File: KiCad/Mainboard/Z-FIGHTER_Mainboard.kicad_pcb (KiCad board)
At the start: 2 copper layers, 100 x 150 mm, 53 parts, among them IC1 Z80SIO, J1 DB9_Male_MountingHoles, J2 DB9_Male_MountingHoles, J3 USB_B, J4 Conn_02x13_Odd_Even, J5 Conn_Parallel_User, J6 Conn_PATA, J7 Conn_02x03_Odd_Even, SW1 SW_Push, SW2 SW_DIP_x03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

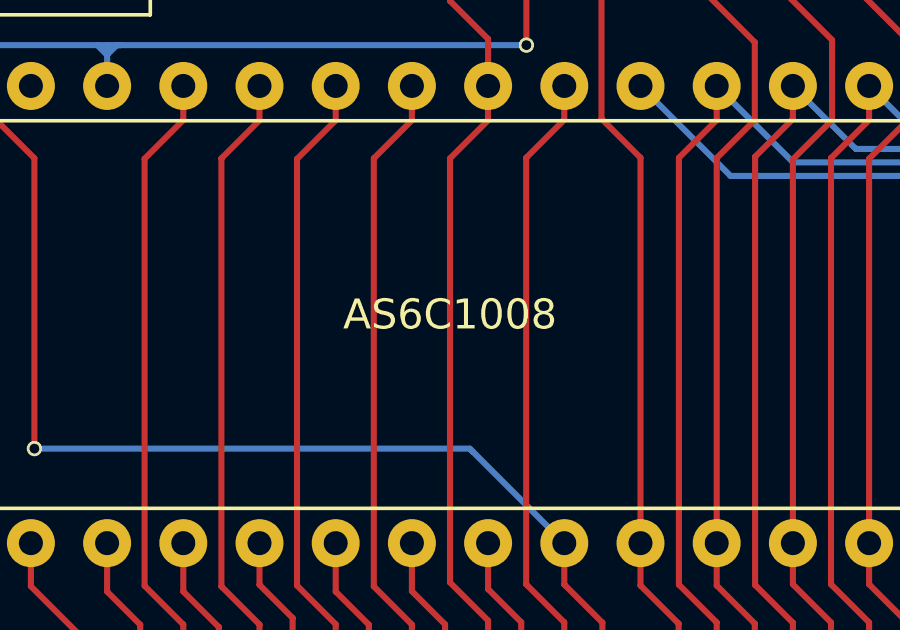
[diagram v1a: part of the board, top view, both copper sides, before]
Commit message: Changed SRAM silkscreen back to '4008
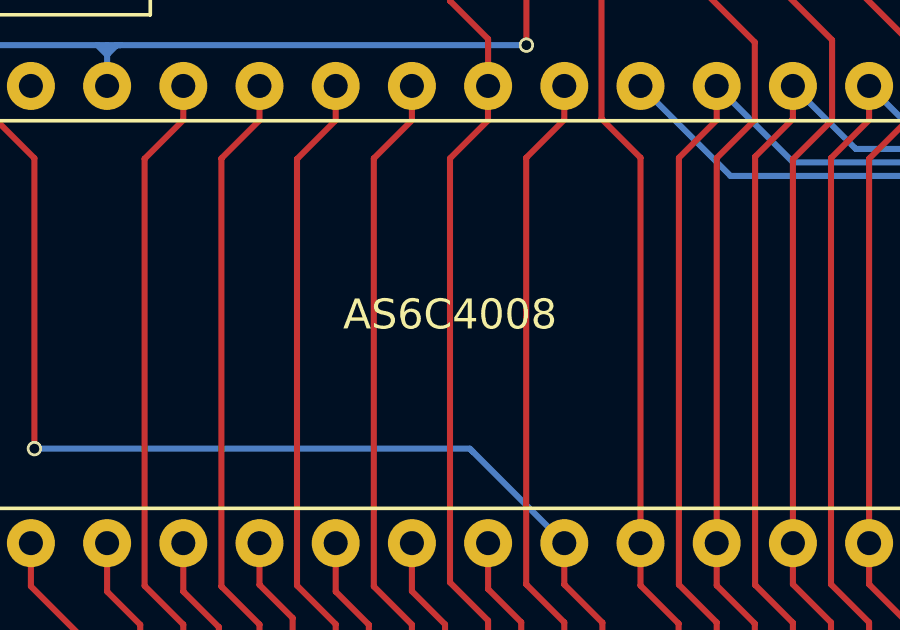
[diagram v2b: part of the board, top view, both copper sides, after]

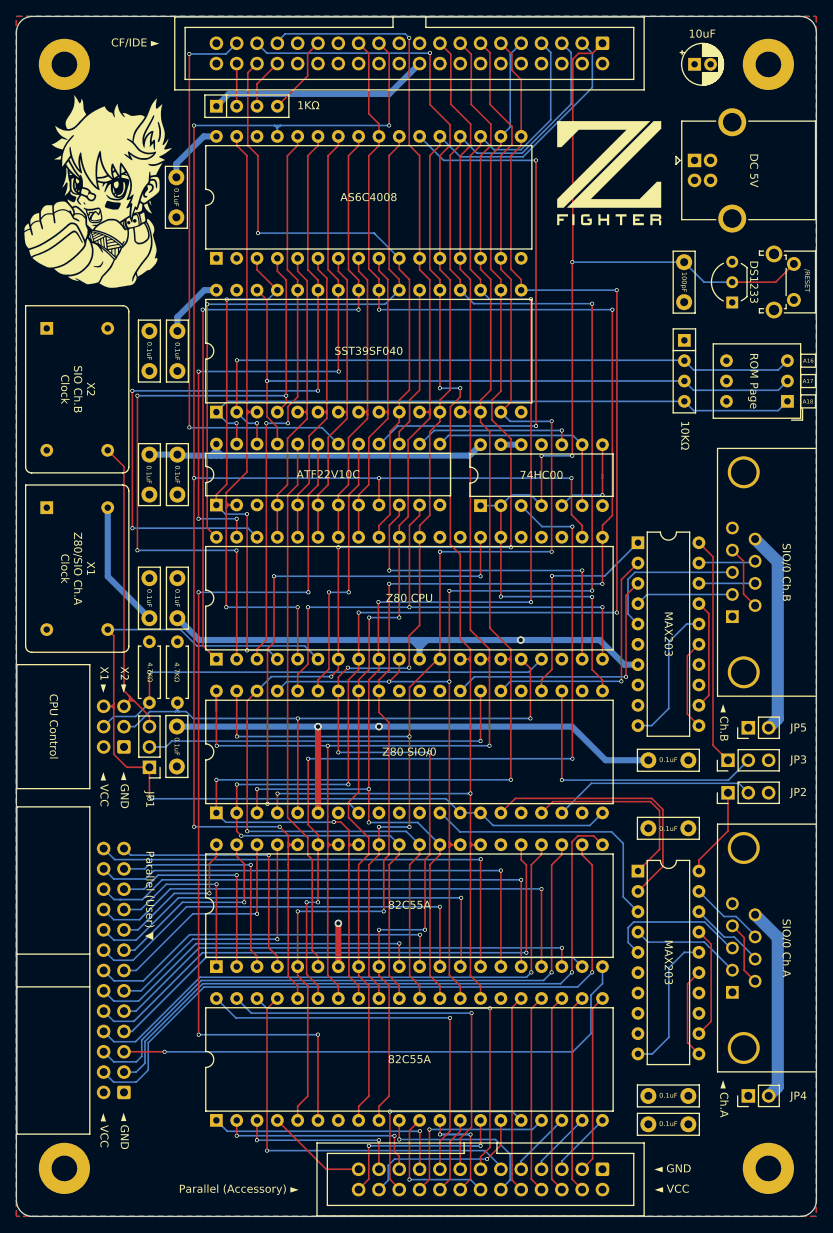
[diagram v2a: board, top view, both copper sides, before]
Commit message: Mainboard improvements
Support for DIP-8 oscillators, replaced system clock pin on CPU control header with CPU #WAIT, added jumper to select internal/external CLOCK2
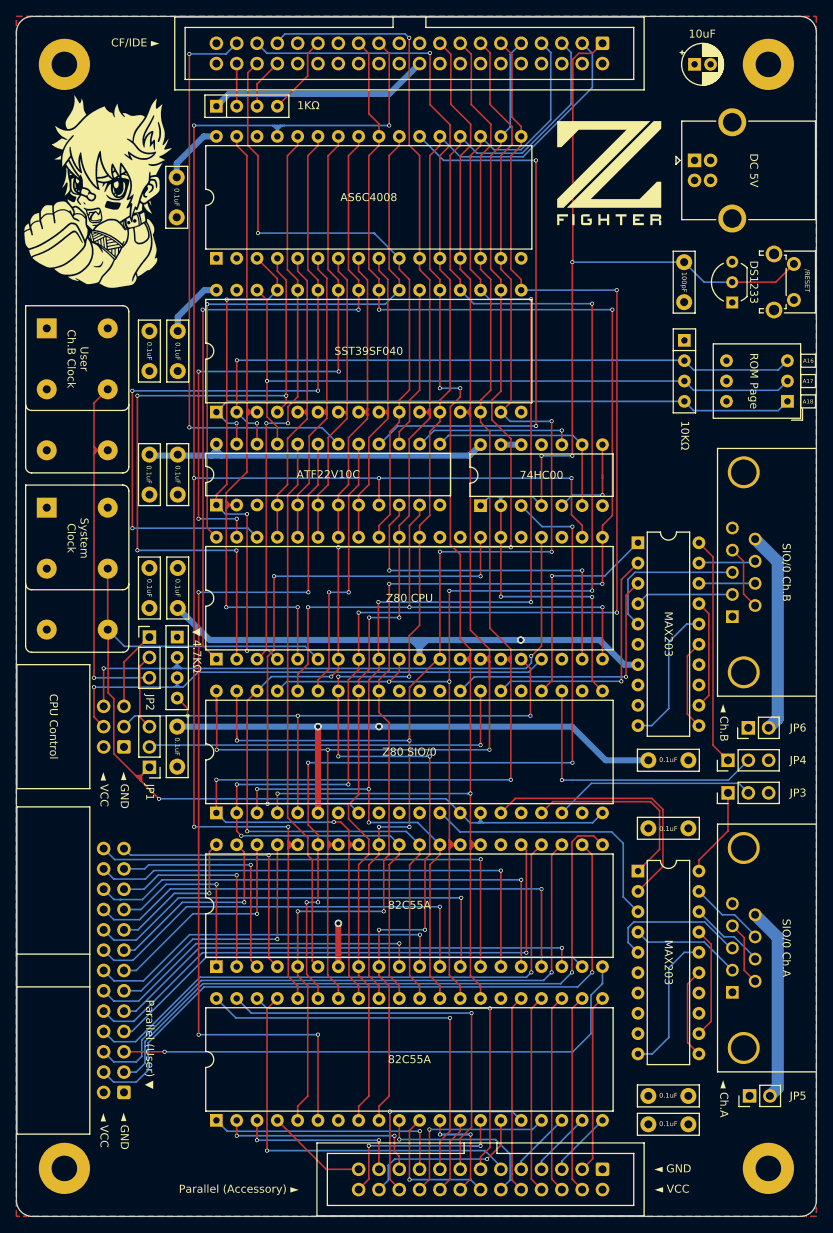
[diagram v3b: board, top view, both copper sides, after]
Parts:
- removed R1, R2: 4.7KΩ, Resistor_THT:R_Axial_DIN0207_L6.3mm_D2.5mm_P7.62mm_Horizontal
- added JP6: Jumper_2_Open, Connector_PinHeader_2.54mm:PinHeader_1x02_P2.54mm_Vertical, F.Cu at (159.4, 115.9)
- added REF**: Oscillator_DIP-8_LargePads, Oscillator:Oscillator_DIP-8_LargePads, F.Cu at (71.7, 88.4)
- added REF**: Oscillator_DIP-8_LargePads, Oscillator:Oscillator_DIP-8_LargePads, F.Cu at (71.7, 66.0)
- added ▼ 4.7KΩ: 4.7KΩ, Resistor_THT:R_Array_SIP4, F.Cu at (88.0, 104.6)
- JP4: value Jumper_2_Open -> Jumper_3_Open; footprint Connector_PinHeader_2.54mm:PinHeader_1x02_P2.54mm_Vertical -> Connector_PinHeader_2.54mm:PinHeader_1x03_P2.54mm_Vertical
- U1: value AS6C1008-55PCN -> AS6C4008-55PCN
- X1, X2: footprint Oscillator:Oscillator_DIP-14 -> Oscillator:Oscillator_DIP-14_LargePads
- moved JP2 74.9 mm to (84.5, 104.6), turned to 0 degrees
- moved JP5 46.0 mm to (159.6, 161.9)
- moved JP4 42.0 mm to (156.9, 120.0)
- moved JP3 4.08 mm to (156.9, 124.1)
- moved C8 1.27 mm to (88.1, 101.0)
- moved C3 1.27 mm to (84.5, 101.0)
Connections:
- net SIOCLOCKB renamed CLOCK_Ch.B
- IC1 pad 13: CLOCK1 -> CLOCK
- IC1 pad 14: CLOCK1 -> CLOCK
- IC1 pad 20: CLOCK1 -> CLOCK
- J7 pad 5: CLOCK2 -> CLOCK2_EXT
- J7 pad 6: CLOCK1 -> #WAIT
- JP1 pad 1: CLOCK1 -> CLOCK
- JP1 pad 3: CLOCK2 -> CLOCK2_USER
- JP2 pad 1: CTSA -> CLOCK2_EXT
- JP2 pad 2: SIO_CTSA -> CLOCK2_USER
- JP2 pad 3: GND -> CLOCK2
- JP3 pad 1: CTSB -> CTSA
- JP3 pad 2: SIO_CTSB -> SIO_CTSA
- JP4 pad 1: VCC -> CTSB
- JP4 pad 2: Net-(J1-Pad9) -> SIO_CTSB
- JP5 pad 2: Net-(J2-Pad9) -> Net-(J1-Pad9)
- U2 pad 24: VCC -> #WAIT
- U2 pad 6: CLOCK1 -> CLOCK
- X1 pad 8: CLOCK1 -> CLOCK
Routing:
- net CLOCK: track 0.00 -> 124.7 mm, vias 0 -> 1
- net CLOCK1: track 113.3 -> 0.00 mm, vias 1 -> 0
- net #WAIT: track 0.00 -> 80.8 mm, vias 0 -> 2
- net VCC: track 242.6 -> 227.0 mm
- net D0: track 173.3 -> 183.3 mm
- net CLOCK2_EXT: track 0.00 -> 9.97 mm
- net CLOCK2_USER: track 0.00 -> 9.64 mm
- net CLOCK2: track 39.4 -> 48.5 mm, vias 0 -> 1
- net D7: track 174.2 -> 182.5 mm
- net #WR: track 218.8 -> 225.8 mm
- net D1: track 180.6 -> 186.2 mm
- net A15: track 80.3 -> 85.0 mm
- net #NMI: track 60.8 -> 65.2 mm
- net #RESET: track 137.6 -> 141.0 mm
- net D6: track 195.9 -> 199.2 mm
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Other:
- board text added: "Mainboard Rev. 2b"
- board text added: "System Clock"
- board text added: "User Ch.B Clock"
- board text removed: "Mainboard Rev. 2a"
- board text removed: "X1 Z80/SIO Ch.A Clock"
- board text removed: "X1 ►"
- board text removed: "X2 SIO Ch.B Clock"
- board text removed: "X2 ►"

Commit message: Gerber settings
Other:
- rule pad_to_mask_clearance: 0.051 -> 0

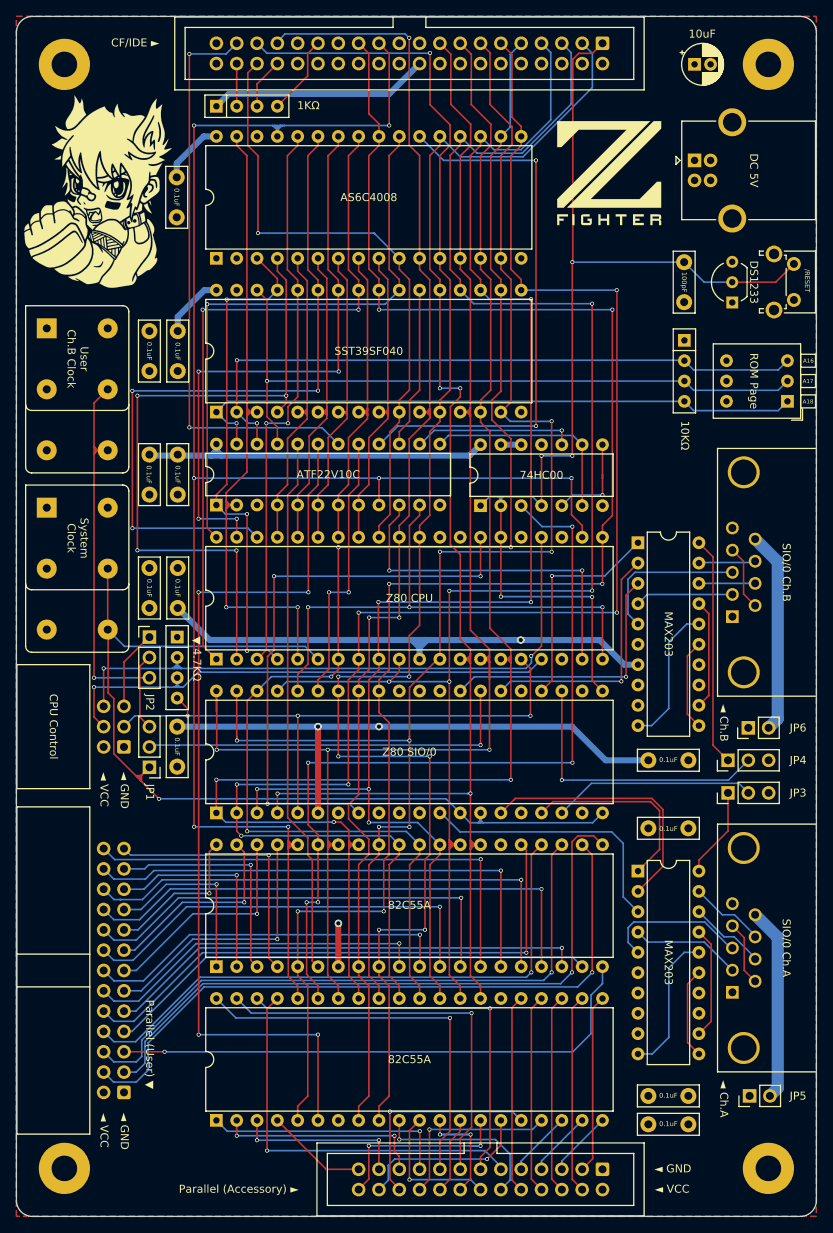
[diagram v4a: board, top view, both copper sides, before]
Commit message: Fixed DIP-8 oscillator support
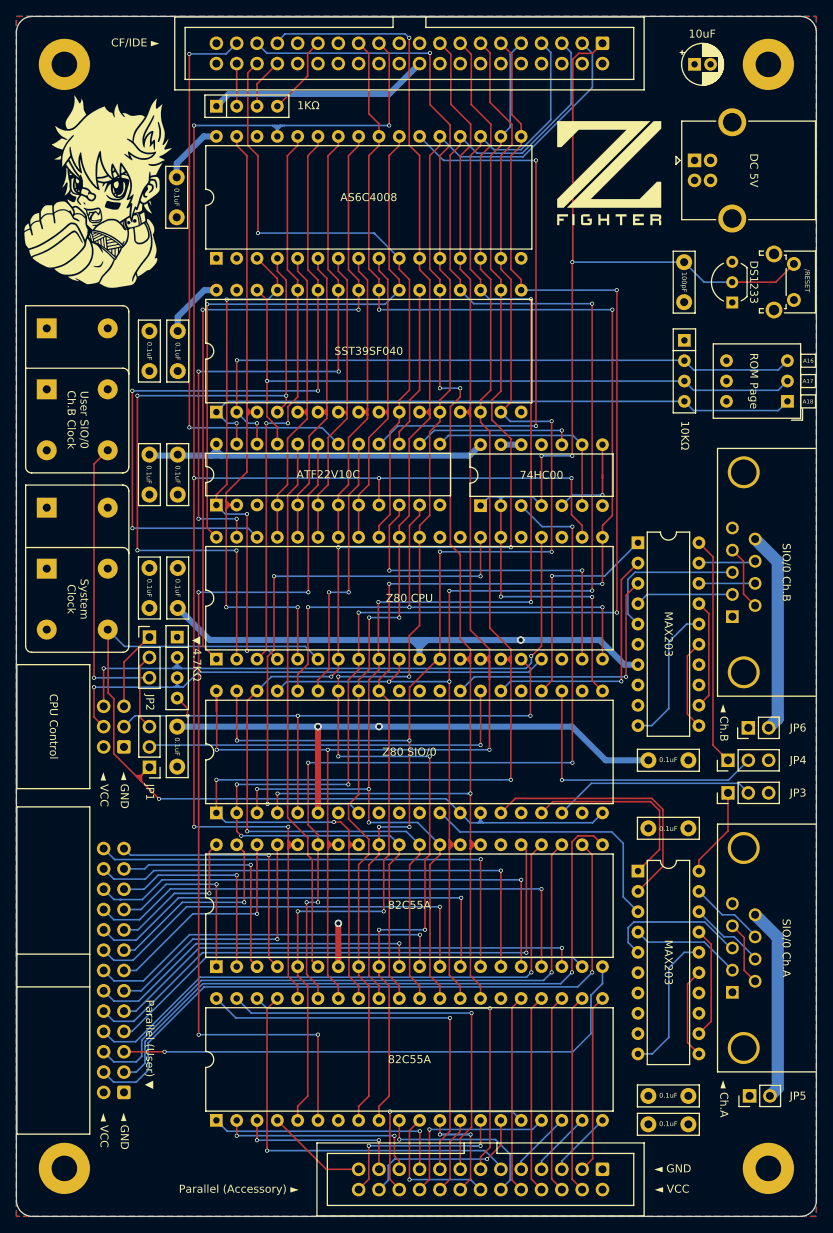
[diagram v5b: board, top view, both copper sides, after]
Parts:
- removed the REF** at (71.7, 88.4)
- removed the REF** at (71.7, 66.0)
- added REF**: Oscillator_DIP-8_LargePads, Oscillator:Oscillator_DIP-8_LargePads, F.Cu at (71.7, 96.0)
- added REF**: Oscillator_DIP-8_LargePads, Oscillator:Oscillator_DIP-8_LargePads, F.Cu at (71.7, 73.6)
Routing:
- net CLOCK2: track 48.5 -> 36.0 mm
- net CLOCK: track 124.7 -> 117.1 mm
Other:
- board text added: "User SIO/0 Ch.B Clock"
- board text removed: "User Ch.B Clock"

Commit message: Flipped X1 bypass cap, tiny routing tweaks
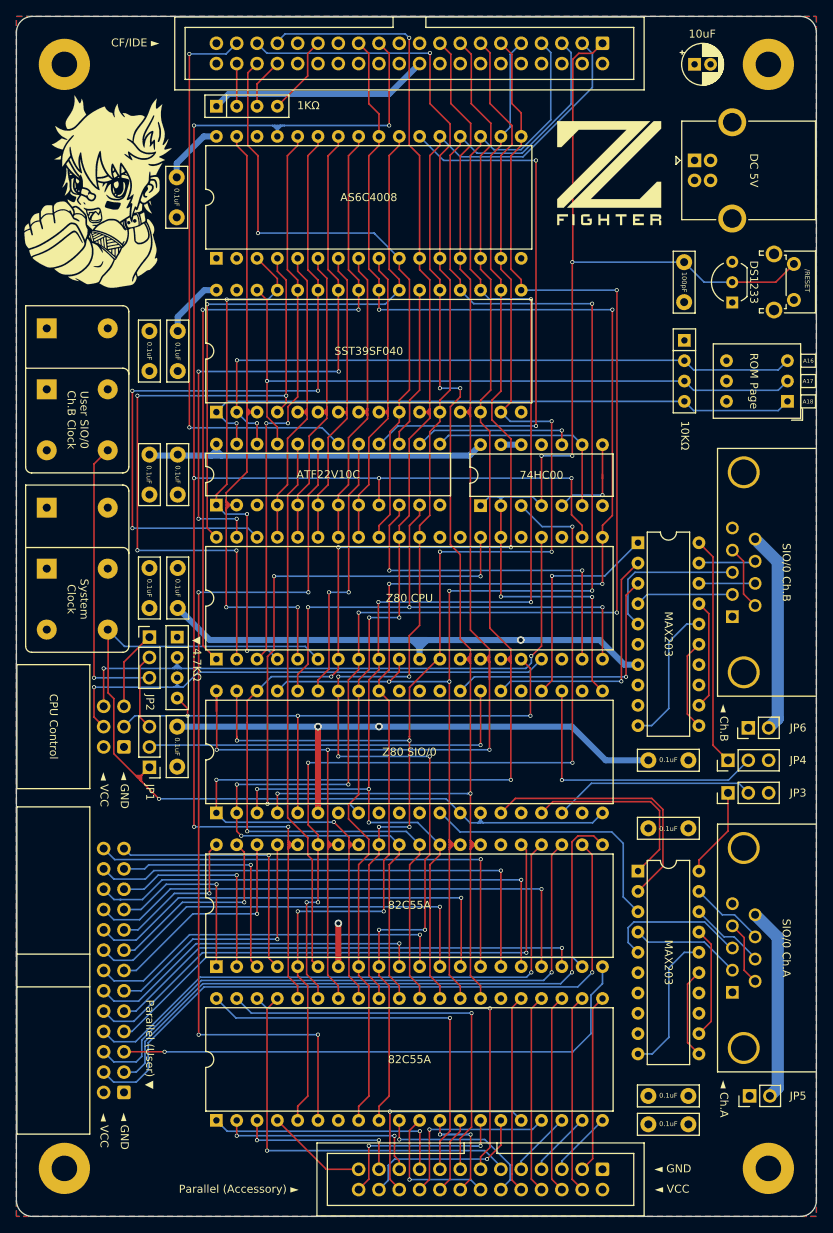
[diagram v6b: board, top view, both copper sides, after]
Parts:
- moved C3 5.00 mm to (84.5, 96.0), turned to 270 degrees
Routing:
- net PC7S: track 21.8 -> 21.1 mm
- net D1: track 186.2 -> 185.7 mm
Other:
- board text added: "Mainboard Rev. 2c"
- board text removed: "Mainboard Rev. 2b"

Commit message: Improved JP1, JP2
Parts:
- RN1: renamed from ▼ 4.7KΩ
- moved JP1 5.08 mm to (84.5, 115.8), turned to 0 degrees
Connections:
- JP1 pad 1: CLOCK -> CLOCK2_USER
- JP1 pad 3: CLOCK2_USER -> CLOCK
- JP2 pad 1: CLOCK2_EXT -> CLOCK2
- JP2 pad 3: CLOCK2 -> CLOCK2_EXT
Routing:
- net CLOCK2: track 36.0 -> 28.3 mm, vias 1 -> 0
- net CLOCK2_EXT: track 9.97 -> 6.86 mm, vias 0 -> 1
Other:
- board text added: "▼ 4.7KΩ"

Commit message: Routing
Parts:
- moved C11 5.08 mm to (88.0, 120.9), turned to 90 degrees
- moved C12 0.88 mm to (146.9, 120.9)
- moved C13 0.78 mm to (151.9, 129.3)
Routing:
- net VCC: track 227.0 -> 161.4 mm, vias 3 -> 4
- net A12: track 84.0 -> 76.3 mm
- net A8: track 89.2 -> 82.4 mm
- net CLOCK: track 117.1 -> 123.7 mm
- net #NMI: track 65.2 -> 62.8 mm
- net GND: track 8.50 -> 6.29 mm
- net A1: track 166.0 -> 164.2 mm, vias 3 -> 4
- net PATA29: track 10.2 -> 11.5 mm
- net D4: track 175.2 -> 176.2 mm
